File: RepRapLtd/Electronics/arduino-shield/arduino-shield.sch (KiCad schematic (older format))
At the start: 7 parts, among them J1 Conn_01x03, J2 Conn_01x03, J3 Conn_01x03, J4 Conn_01x03, J5 Conn_01x03, J6 Conn_01x03

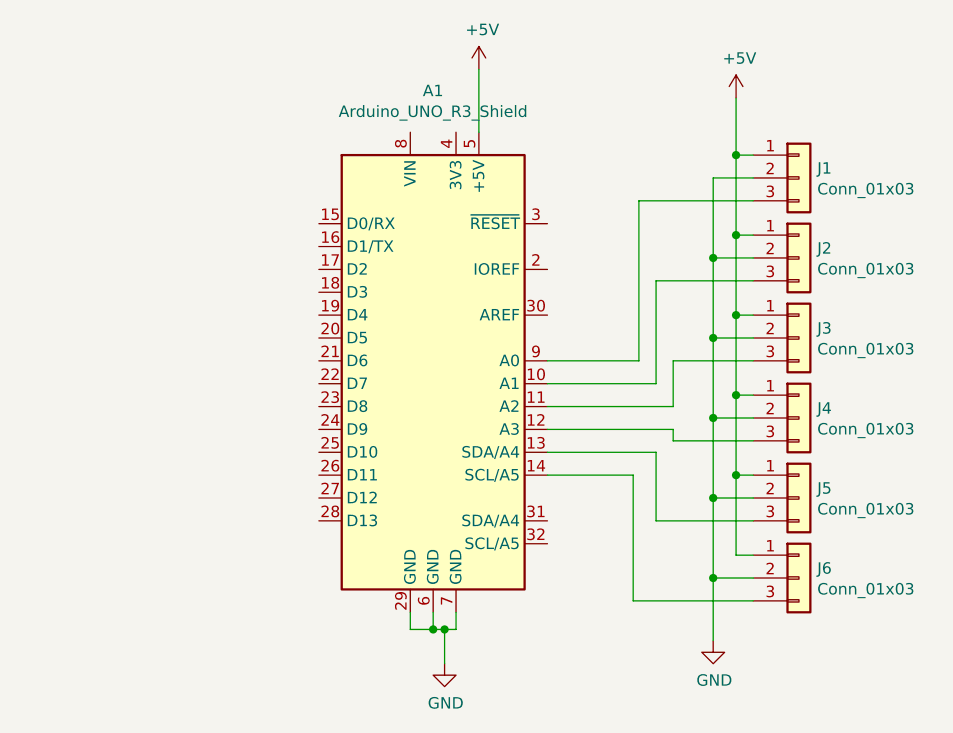
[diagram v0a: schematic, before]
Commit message: Added button connectors and LED connector to the Arduino shield.
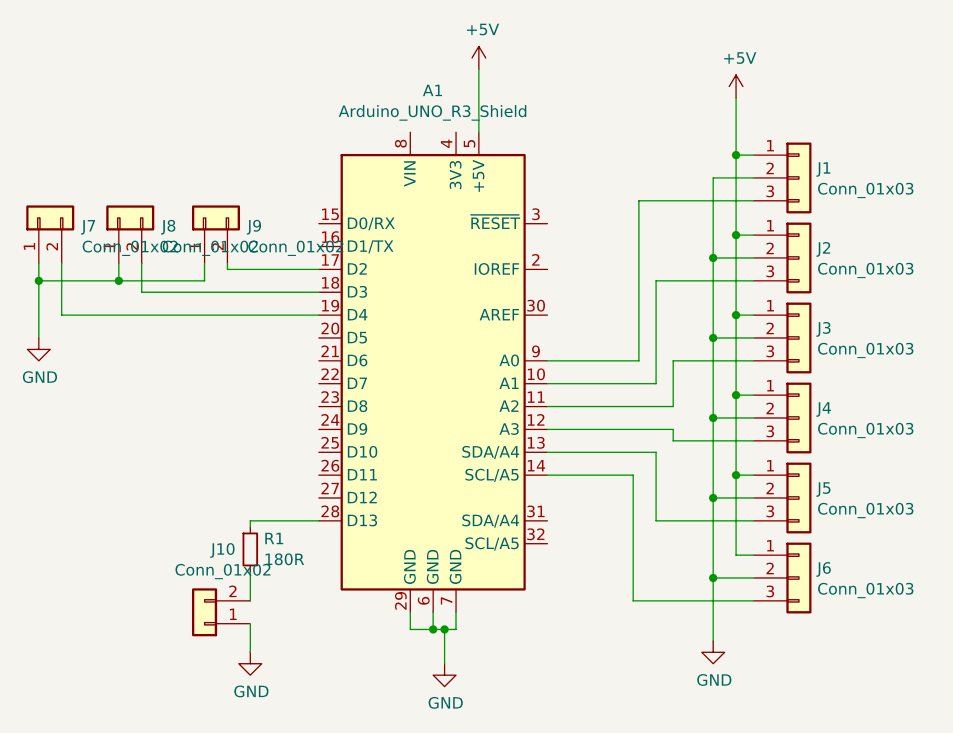
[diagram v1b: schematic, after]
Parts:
- added J10, J7, J8, J9: Conn_01x02, Connector_PinHeader_2.54mm:PinHeader_1x02_P2.54mm_Vertical, symbol Connector_Generic:Conn_01x02
- added R1: 180R, Resistor_SMD:R_0805_2012Metric, symbol Device:R_Small
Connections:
- net GND: now also J10.1 (Pin_1), J7.1 (Pin_1), J8.1 (Pin_1), J9.1 (Pin_1)
- net at A1.17 (D2): now also J9.2 (Pin_2)
- net at A1.18 (D3): now also J8.2 (Pin_2)
- net at A1.19 (D4): now also J7.2 (Pin_2)
- net at A1.28 (D13): now also R1.1
- new net: J10.2 (Pin_2), R1.2
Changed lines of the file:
@@
 	4975 3575 5150 3575
 Connection ~ 4975 3925
+$Comp
+L Connector_Generic:Conn_01x02 J9
+U 1 1 60BE4CB8
+P 2750 3750
+F 0 "J9" V 2714 3562 50  0000 R CNN
+F 1 "Conn_01x02" V 2623 3562 50  0000 R CNN
+F 2 "Connector_PinHeader_2.54mm:PinHeader_1x02_P2.54mm_Vertical" H 2750 3750 50  0001 C CNN
+F 3 "~" H 2750 3750 50  0001 C CNN
+	1    2750 3750
+	0    -1   -1   0
+$EndComp
+$Comp
+L Connector_Generic:Conn_01x02 J8
+U 1 1 60BE5F6E
+P 2375 3750
+F 0 "J8" V 2339 3562 50  0000 R CNN
+F 1 "Conn_01x02" V 2248 3562 50  0000 R CNN
+F 2 "Connector_PinHeader_2.54mm:PinHeader_1x02_P2.54mm_Vertical" H 2375 3750 50  0001 C CNN
+F 3 "~" H 2375 3750 50  0001 C CNN
+	1    2375 3750
+	0    -1   -1   0
+$EndComp
+$Comp
+L Connector_Generic:Conn_01x02 J7
+U 1 1 60BE658F
+P 2025 3750
+F 0 "J7" V 1989 3562 50  0000 R CNN
+F 1 "Conn_01x02" V 1898 3562 50  0000 R CNN
+F 2 "Connector_PinHeader_2.54mm:PinHeader_1x02_P2.54mm_Vertical" H 2025 3750 50  0001 C CNN
+F 3 "~" H 2025 3750 50  0001 C CNN
+	1    2025 3750
+	0    -1   -1   0
+$EndComp
+Wire Wire Line
+	2850 3950 2850 3975
+Wire Wire Line
+	2850 3975 3250 3975
+Wire Wire Line
+	2475 3950 2475 4075
+Wire Wire Line
+	2475 4075 3250 4075
+Wire Wire Line
+	2125 3950 2125 4175
+Wire Wire Line
+	2125 4175 3250 4175
+Wire Wire Line
+	2750 3950 2750 4025
+Wire Wire Line
+	2750 4025 2375 4025
+Wire Wire Line
+	2375 4025 2375 3950
+Wire Wire Line
+	2375 4025 2025 4025
+Wire Wire Line
+	2025 4025 2025 3950
+Connection ~ 2375 4025
+$Comp
+L power:GND #PWR0105
+U 1 1 60BED2CC
+P 2025 4275
+F 0 "#PWR0105" H 2025 4025 50  0001 C CNN
+F 1 "GND" H 2030 4102 50  0000 C CNN
+F 2 "" H 2025 4275 50  0001 C CNN
+F 3 "" H 2025 4275 50  0001 C CNN
+	1    2025 4275
+	1    0    0    -1
+$EndComp
+Wire Wire Line
+	2025 4025 2025 4275
+Connection ~ 2025 4025
+$Comp
+L Device:R_Small R1
+U 1 1 60BEF562
+P 2950 5200
+F 0 "R1" H 3009 5246 50  0000 L CNN
+F 1 "180R" H 3009 5155 50  0000 L CNN
+F 2 "Resistor_SMD:R_0805_2012Metric" H 2950 5200 50  0001 C CNN
+F 3 "~" H 2950 5200 50  0001 C CNN
+	1    2950 5200
+	1    0    0    -1
+$EndComp
+Wire Wire Line
+	3250 5075 2950 5075
+Wire Wire Line
+	2950 5075 2950 5100
+$Comp
+L Connector_Generic:Conn_01x02 J10
+U 1 1 60BF1843
+P 2750 5525
+F 0 "J10" H 2668 5200 50  0000 C CNN
+F 1 "Conn_01x02" H 2668 5291 50  0000 C CNN
+F 2 "Connector_PinHeader_2.54mm:PinHeader_1x02_P2.54mm_Vertical" H 2750 5525 50  0001 C CNN
+F 3 "~" H 2750 5525 50  0001 C CNN
+	1    2750 5525
+	-1   0    0    1
+$EndComp
+Wire Wire Line
+	2950 5300 2950 5425
+$Comp
+L power:GND #PWR0106
+U 1 1 60BF35E8
+P 2950 5650
+F 0 "#PWR0106" H 2950 5400 50  0001 C CNN
+F 1 "GND" H 2955 5477 50  0000 C CNN
+F 2 "" H 2950 5650 50  0001 C CNN
+F 3 "" H 2950 5650 50  0001 C CNN
+	1    2950 5650
+	1    0    0    -1
+$EndComp
+Wire Wire Line
+	2950 5525 2950 5650
 $EndSCHEMATC

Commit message: 3-axis integrated design for all torques added.
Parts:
- A1: symbol reprapltd-kicad:Arduino_UNO_R3_Shield -> arduino-shield-rescue:Arduino_UNO_R3_Shield-reprapltd-kicad
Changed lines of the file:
@@
 $EndDescr
 $Comp
-L reprapltd-kicad:Arduino_UNO_R3_Shield A1
+L arduino-shield-rescue:Arduino_UNO_R3_Shield-reprapltd-kicad A1
 U 1 1 60BE011A
 P 3750 4375
